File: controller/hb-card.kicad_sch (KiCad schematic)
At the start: 21 parts, among them J4 Conn_01x14

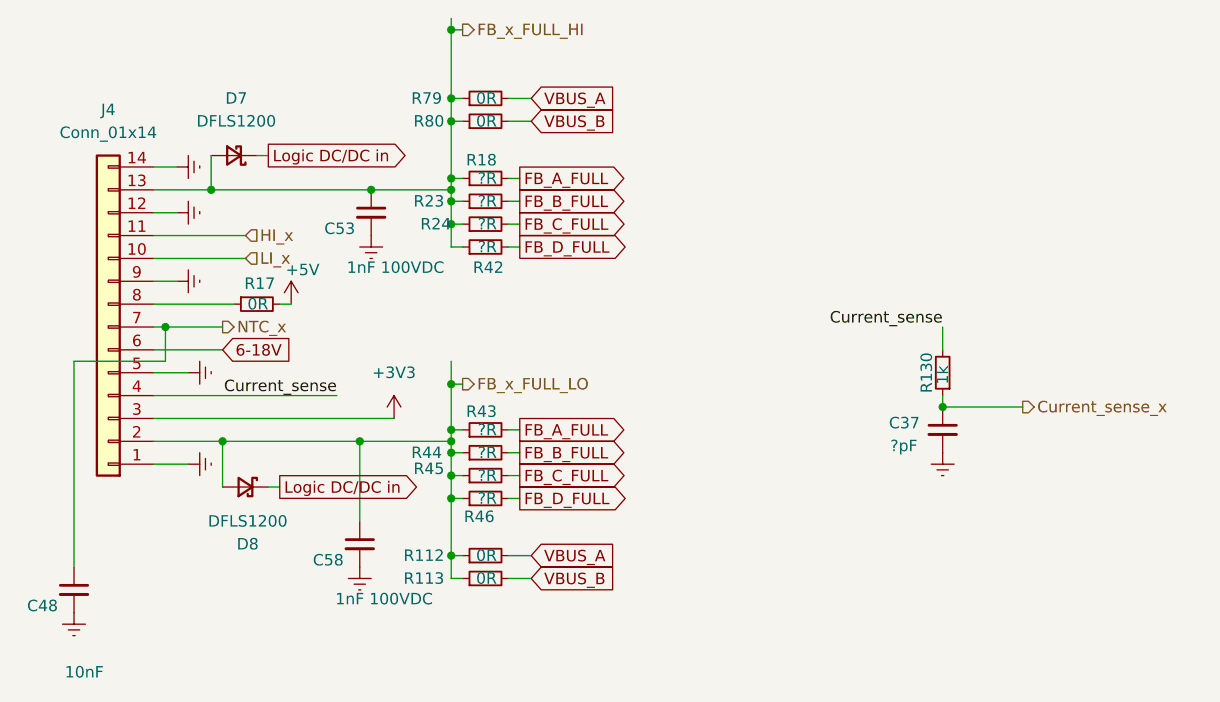
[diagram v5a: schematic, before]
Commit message: Controller - Expand to 100x50mm to allow VBUS to go around
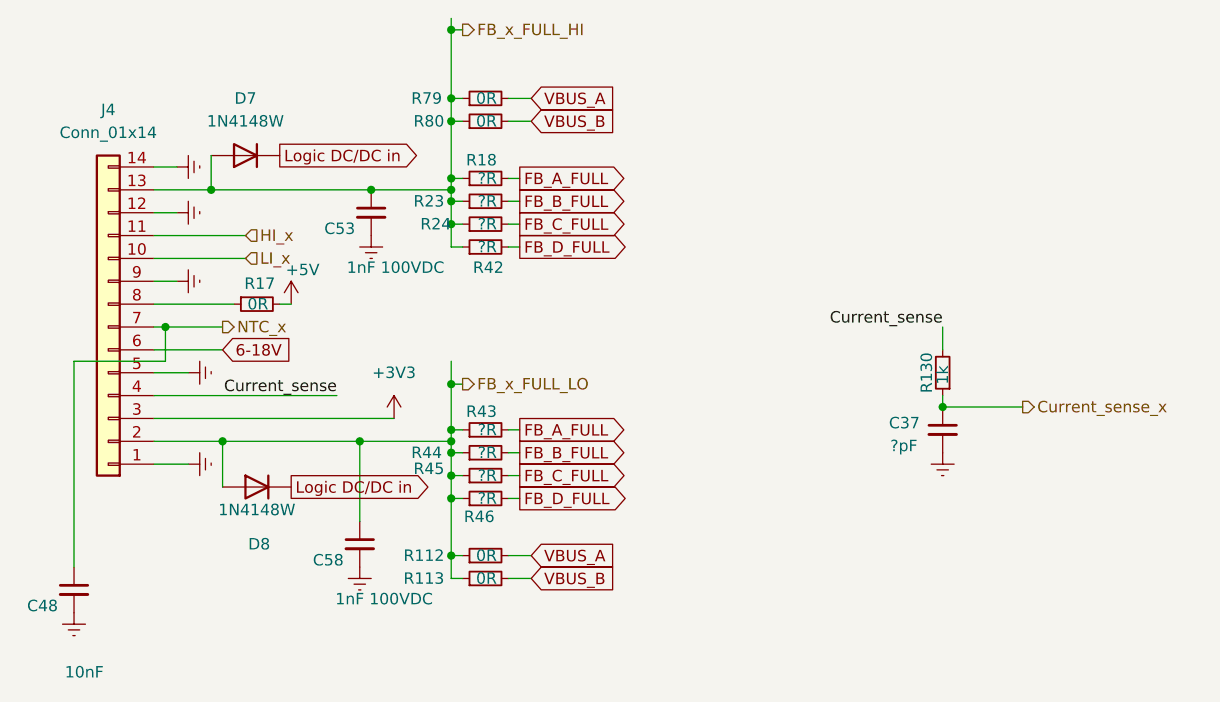
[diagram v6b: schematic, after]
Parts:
- D7, D8: value DFLS1200 -> 1N4148W; footprint Diode_SMD:D_PowerDI-123 -> Diode_SMD:D_SOD-123; symbol Device:D_Schottky_Small -> Diode:1N4148W
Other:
- moved on the sheet: D7, D8
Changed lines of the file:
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@@
 	(paper "A4")
+	(junction
+		(at 73.66 92.71)
+		(diameter 0)
+		(color 0 0 0 0)
+	)
+	(junction
+		(at 128.27 85.09)
+		(diameter 0)
+		(color 0 0 0 0)
+	)
+	(junction
+		(at 73.66 59.69)
+		(diameter 0)
+		(color 0 0 0 0)
+	)
+	(junction
+		(at 73.66 87.63)
+		(diameter 0)
+		(color 0 0 0 0)
+	)
+	(junction
+		(at 73.66 95.25)
+		(diameter 0)
+		(color 0 0 0 0)
+	)
+	(junction
+		(at 73.66 64.77)
+		(diameter 0)
+		(color 0 0 0 0)
+	)
+	(junction
+		(at 73.66 101.6)
+		(diameter 0)
+		(color 0 0 0 0)
+	)
+	(junction
+		(at 73.66 62.23)
+		(diameter 0)
+		(color 0 0 0 0)
+	)
+	(junction
+		(at 73.66 90.17)
+		(diameter 0)
+		(color 0 0 0 0)
+	)
+	(junction
+		(at 73.66 53.34)
+		(diameter 0)
+		(color 0 0 0 0)
+	)
+	(junction
+		(at 41.91 76.2)
+		(diameter 0)
+		(color 0 0 0 0)
+	)
+	(junction
+		(at 46.99 60.96)
+		(diameter 0)
+		(color 0 0 0 0)
+	)
+	(junction
+		(at 73.66 60.96)
+		(diameter 0)
+		(color 0 0 0 0)
+	)
 	(junction
 		(at 48.26 88.9)
@@
 	)
 	(junction
-		(at 46.99 60.96)
-		(diameter 0)
-		(color 0 0 0 0)
-	)
-	(junction
-		(at 73.66 92.71)
-		(diameter 0)
-		(color 0 0 0 0)
-	)
-	(junction
-		(at 128.27 85.09)
-		(diameter 0)
-		(color 0 0 0 0)
-	)
-	(junction
-		(at 73.66 59.69)
-		(diameter 0)
-		(color 0 0 0 0)
-	)
-	(junction
-		(at 73.66 87.63)
-		(diameter 0)
-		(color 0 0 0 0)
-	)
-	(junction
-		(at 73.66 95.25)
-		(diameter 0)
-		(color 0 0 0 0)
-	)
-	(junction
-		(at 73.66 64.77)
-		(diameter 0)
-		(color 0 0 0 0)
-	)
-	(junction
-		(at 73.66 101.6)
-		(diameter 0)
-		(color 0 0 0 0)
-	)
-	(junction
-		(at 73.66 62.23)
-		(diameter 0)
-		(color 0 0 0 0)
-	)
-	(junction
-		(at 73.66 90.17)
-		(diameter 0)
-		(color 0 0 0 0)
-	)
-	(junction
-		(at 73.66 53.34)
-		(diameter 0)
-		(color 0 0 0 0)
-	)
-	(junction
-		(at 41.91 76.2)
-		(diameter 0)
-		(color 0 0 0 0)
-	)
-	(junction
-		(at 73.66 60.96)
-		(diameter 0)
-		(color 0 0 0 0)
-	)
-	(junction
 		(at 73.66 50.8)
 		(diameter 0)
@@
 	(wire
 		(pts
+			(xy 48.26 88.9) (xy 63.5 88.9)
+		)
+		(stroke
+			(width 0)
+			(type default)
+		)
+	)
+	(wire
+		(pts
 			(xy 73.66 64.77) (xy 73.66 62.23)
 		)
@@
 	(wire
 		(pts
-			(xy 48.26 88.9) (xy 63.5 88.9)
+			(xy 46.99 60.96) (xy 64.77 60.96)
 		)
 		(stroke
@@
 	(wire
 		(pts
-			(xy 53.34 93.98) (xy 54.61 93.98)
-		)
-		(stroke
-			(width 0)
-			(type default)
-		)
-	)
-	(wire
-		(pts
 			(xy 73.66 88.9) (xy 73.66 90.17)
 		)
@@
 	(wire
 		(pts
-			(xy 52.07 57.15) (xy 53.34 57.15)
-		)
-		(stroke
-			(width 0)
-			(type default)
-		)
-	)
-	(wire
-		(pts
 			(xy 73.66 59.69) (xy 74.93 59.69)
 		)
@@
 		(pts
 			(xy 73.66 101.6) (xy 74.93 101.6)
-		)
-		(stroke
-			(width 0)
-			(type default)
-		)
-	)
-	(wire
-		(pts
-			(xy 46.99 60.96) (xy 64.77 60.96)
 		)
 		(stroke
@@
 	(global_label "Logic DC{slash}DC in"
 		(shape output)
-		(at 53.34 57.15 0)
+		(at 54.61 57.15 0)
 		(fields_autoplaced yes)
 		(effects
@@
 		)
 		(property "Intersheetrefs" "${INTERSHEET_REFS}"
-			(at 71.4442 57.15 0)
+			(at 72.7142 57.15 0)
 			(effects
 				(font
@@
 	(global_label "Logic DC{slash}DC in"
 		(shape output)
-		(at 54.61 93.98 0)
+		(at 55.88 93.98 0)
 		(fields_autoplaced yes)
 		(effects
@@
 		)
 		(property "Intersheetrefs" "${INTERSHEET_REFS}"
-			(at 72.7142 93.98 0)
+			(at 73.9842 93.98 0)
 			(effects
 				(font
@@
 	)
 	(symbol
-		(lib_id "Device:D_Schottky_Small")
-		(at 49.53 57.15 180)
+		(lib_id "Diode:1N4148W")
+		(at 50.8 57.15 180)
 		(unit 1)
-		(exclude_from_sim yes)
+		(exclude_from_sim no)
 		(in_bom yes)
 		(on_board yes)
@@
 		(fields_autoplaced yes)
 		(property "Reference" "D7"
-			(at 49.784 50.8 0)
-			(effects
-				(font
-					(size 1.27 1.27)
-				)
-			)
-		)
-		(property "Value" "DFLS1200"
-			(at 49.784 53.34 0)
-			(effects
-				(font
-					(size 1.27 1.27)
-				)
-			)
-		)
-		(property "Footprint" "Diode_SMD:D_PowerDI-123"
-			(at 49.53 57.15 90)
-			(effects
-				(font
-					(size 1.27 1.27)
-				)
-				(hide yes)
-			)
-		)
-		(property "Datasheet" "~"
-			(at 49.53 57.15 90)
-			(effects
-				(font
-					(size 1.27 1.27)
-				)
-				(hide yes)
-			)
-		)
-		(property "Description" ""
-			(at 49.53 57.15 0)
+			(at 50.8 50.8 0)
+			(effects
+				(font
+					(size 1.27 1.27)
+				)
+			)
+		)
+		(property "Value" "1N4148W"
+			(at 50.8 53.34 0)
+			(effects
+				(font
+					(size 1.27 1.27)
+				)
+			)
+		)
+		(property "Footprint" "Diode_SMD:D_SOD-123"
+			(at 50.8 52.705 0)
+			(effects
+				(font
+					(size 1.27 1.27)
+				)
+				(hide yes)
+			)
+		)
+		(property "Datasheet" "https://www.vishay.com/docs/85748/1n4148w.pdf"
+			(at 50.8 57.15 0)
+			(effects
+				(font
+					(size 1.27 1.27)
+				)
+				(hide yes)
+			)
+		)
+		(property "Description" "75V 0.15A Fast Switching Diode, SOD-123"
+			(at 50.8 57.15 0)
 			(effects
 				(font
@@
 		)
 		(property "Sim.Library" "/home/albin/hw-half-bridge/sim/Diodes/DFLS1200.spice.txt"
-			(at 49.53 57.15 0)
+			(at 50.8 57.15 0)
 			(effects
 				(font
@@
 		)
 		(property "Sim.Name" "DI_DFLS1200"
-			(at 49.53 57.15 0)
+			(at 50.8 57.15 0)
 			(effects
 				(font
@@
 		)
 		(property "Sim.Device" "D"
-			(at 49.53 57.15 0)
+			(at 50.8 57.15 0)
 			(effects
 				(font
@@
 		)
 		(property "Sim.Pins" "1=K 2=A"
-			(at 49.53 57.15 0)
+			(at 50.8 57.15 0)
 			(effects
 				(font
@@
 		)
 		(property "Sim.Params" "temp=50"
-			(at 49.53 57.15 0)
+			(at 50.8 57.15 0)
 			(effects
 				(font
@@
 	)
 	(symbol
-		(lib_id "Device:D_Schottky_Small")
-		(at 50.8 93.98 0)
+		(lib_id "Diode:1N4148W")
+		(at 52.07 93.98 0)
 		(mirror y)
 		(unit 1)
-		(exclude_from_sim yes)
+		(exclude_from_sim no)
 		(in_bom yes)
 		(on_board yes)
 		(dnp no)
 		(property "Reference" "D8"
-			(at 51.054 100.33 0)
-			(effects
-				(font
-					(size 1.27 1.27)
-				)
-			)
-		)
-		(property "Value" "DFLS1200"
-			(at 51.054 97.79 0)
-			(effects
-				(font
-					(size 1.27 1.27)
-				)
-			)
-		)
-		(property "Footprint" "Diode_SMD:D_PowerDI-123"
-			(at 50.8 93.98 90)
-			(effects
-				(font
-					(size 1.27 1.27)
-				)
-				(hide yes)
-			)
-		)
-		(property "Datasheet" "~"
-			(at 50.8 93.98 90)
-			(effects
-				(font
-					(size 1.27 1.27)
-				)
-				(hide yes)
-			)
-		)
-		(property "Description" ""
-			(at 50.8 93.98 0)
+			(at 52.324 100.33 0)
+			(effects
+				(font
+					(size 1.27 1.27)
+				)
+			)
+		)
+		(property "Value" "1N4148W"
+			(at 52.07 96.52 0)
+			(effects
+				(font
+					(size 1.27 1.27)
+				)
+			)
+		)
+		(property "Footprint" "Diode_SMD:D_SOD-123"
+			(at 52.07 98.425 0)
+			(effects
+				(font
+					(size 1.27 1.27)
+				)
+				(hide yes)
+			)
+		)
+		(property "Datasheet" "https://www.vishay.com/docs/85748/1n4148w.pdf"
+			(at 52.07 93.98 0)
+			(effects
+				(font
+					(size 1.27 1.27)
+				)
+				(hide yes)
+			)
+		)
+		(property "Description" "75V 0.15A Fast Switching Diode, SOD-123"
+			(at 52.07 93.98 0)
 			(effects
 				(font
@@
 		)
 		(property "Sim.Library" "/home/albin/hw-half-bridge/sim/Diodes/DFLS1200.spice.txt"
-			(at 50.8 93.98 0)
+			(at 52.07 93.98 0)
 			(effects
 				(font
@@
 		)
 		(property "Sim.Name" "DI_DFLS1200"
-			(at 50.8 93.98 0)
+			(at 52.07 93.98 0)
 			(effects
 				(font
@@
 		)
 		(property "Sim.Device" "D"
-			(at 50.8 93.98 0)
+			(at 52.07 93.98 0)
 			(effects
 				(font
@@
 		)
 		(property "Sim.Pins" "1=K 2=A"
-			(at 50.8 93.98 0)
+			(at 52.07 93.98 0)
 			(effects
 				(font
@@
 		)
 		(property "Sim.Params" "temp=50"
-			(at 50.8 93.98 0)
-			(effects
-				(font
+			(at 52.07 93.98 0)
+			(effects
+				(font

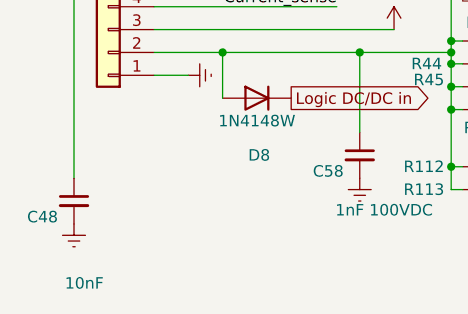
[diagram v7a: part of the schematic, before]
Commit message: controller - Update BOM - WIP
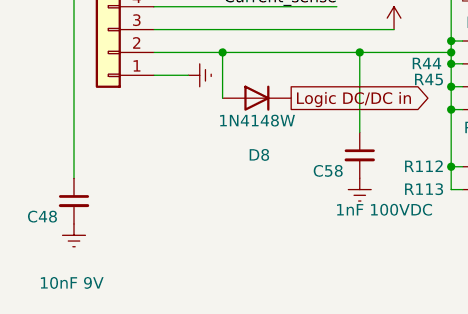
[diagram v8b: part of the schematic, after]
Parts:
- C48: value 10nF -> 10nF 9V
